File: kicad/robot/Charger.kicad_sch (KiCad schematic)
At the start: 32 parts, among them U13 MAX77976EFD+

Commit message: Added stock counts to parts I have
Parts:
- U13: Stock (none) -> 25
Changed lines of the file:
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@@
+      (effects (font (size 1.27 1.27)) hide)
+    )
+    (property "Stock" "25" (id 6) (at 121.92 106.68 0)
       (effects (font (size 1.27 1.27)) hide)
     )

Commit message: Batch BOM edits adding manufactuer and part numbers only
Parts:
- D5: Manufacturer (none) -> Nexperia
- D6: Manufacturer (none) -> Harvatek
- D7: Manufacturer (none) -> Vishay; manufacturer Vishay -> (none)
- L2: Manufacturer (none) -> Vishay
- R49: Manufacturer (none) -> Stackpole Electronics; Part Number (none) -> RMCF0603JG100K
- R50: Manufacturer (none) -> Stackpole Electronics; Part Number (none) -> RMCF0603JJ1K00
- R56: Manufacturer (none) -> Yageo; Part Number (none) -> RC0603JR-07110RL
- TP12: Manufacturer (none) -> N/A
- U13: Manufacturer (none) -> Maxim
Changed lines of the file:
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@@
+      (effects (font (size 1.27 1.27)) hide)
+    )
+    (property "Manufacturer" "Yageo" (id 5) (at 82.55 137.16 0)
+      (effects (font (size 1.27 1.27)) hide)
+    )
+    (property "Part Number" "RC0603JR-07110RL" (id 6) (at 82.55 137.16 0)
       (effects (font (size 1.27 1.27)) hide)
     )
@@
       (effects (font (size 1.27 1.27)) hide)
     )
+    (property "Manufacturer" "N/A" (id 6) (at 50.8 163.83 0)
+      (effects (font (size 1.27 1.27)) hide)
+    )
     (pin "1")
     (pin "2")
@@
     )
     (property "Description" "TVS Diode 20V" (id 5) (at 44.45 87.63 0)
+      (effects (font (size 1.27 1.27)) hide)
+    )
+    (property "Manufacturer" "Nexperia" (id 6) (at 44.45 87.63 0)
       (effects (font (size 1.27 1.27)) hide)
     )
@@
     )
     (property "Stock" "25" (id 6) (at 121.92 106.68 0)
+      (effects (font (size 1.27 1.27)) hide)
+    )
+    (property "Manufacturer" "Maxim" (id 7) (at 121.92 106.68 0)
       (effects (font (size 1.27 1.27)) hide)
     )
@@
       (effects (font (size 1.27 1.27)) hide)
     )
+    (property "Manufacturer" "Harvatek" (id 6) (at 72.39 137.16 0)
+      (effects (font (size 1.27 1.27)) hide)
+    )
     (pin "1")
     (pin "2")
@@
       (effects (font (size 1.27 1.27)) hide)
     )
+    (property "Manufacturer" "Vishay" (id 6) (at 171.45 99.06 0)
+      (effects (font (size 1.27 1.27)) hide)
+    )
     (pin "1")
     (pin "2")
@@
     )
     (property "Datasheet" "~" (id 3) (at 69.85 114.3 0)
+      (effects (font (size 1.27 1.27)) hide)
+    )
+    (property "Manufacturer" "Stackpole Electronics" (id 4) (at 69.85 114.3 0)
+      (effects (font (size 1.27 1.27)) hide)
+    )
+    (property "Part Number" "RMCF0603JG100K" (id 5) (at 69.85 114.3 0)
       (effects (font (size 1.27 1.27)) hide)
     )
@@
       (effects (font (size 1.27 1.27)) hide)
     )
+    (property "Manufacturer" "Stackpole Electronics" (id 4) (at 72.39 144.78 0)
+      (effects (font (size 1.27 1.27)) hide)
+    )
+    (property "Part Number" "RMCF0603JJ1K00" (id 5) (at 72.39 144.78 0)
+      (effects (font (size 1.27 1.27)) hide)
+    )
     (pin "1")
     (pin "2")
@@
       (effects (font (size 1.27 1.27)) (justify left) hide)
     )
-    (property "manufacturer" "Vishay" (id 15) (at 115.57 22.86 0)
+    (property "manufacturer" "" (id 15) (at 115.57 22.86 0)
       (effects (font (size 1.27 1.27)) (justify left) hide)
     )
@@
       (effects (font (size 1.27 1.27)) (justify left) hide)
     )
-    (pin "1")
+    (property "Manufacturer" "Vishay" (id 27) (at 115.57 63.5 0)
+      (effects (font (size 1.27 1.27)) hide)
+    )
+    (pin "1")

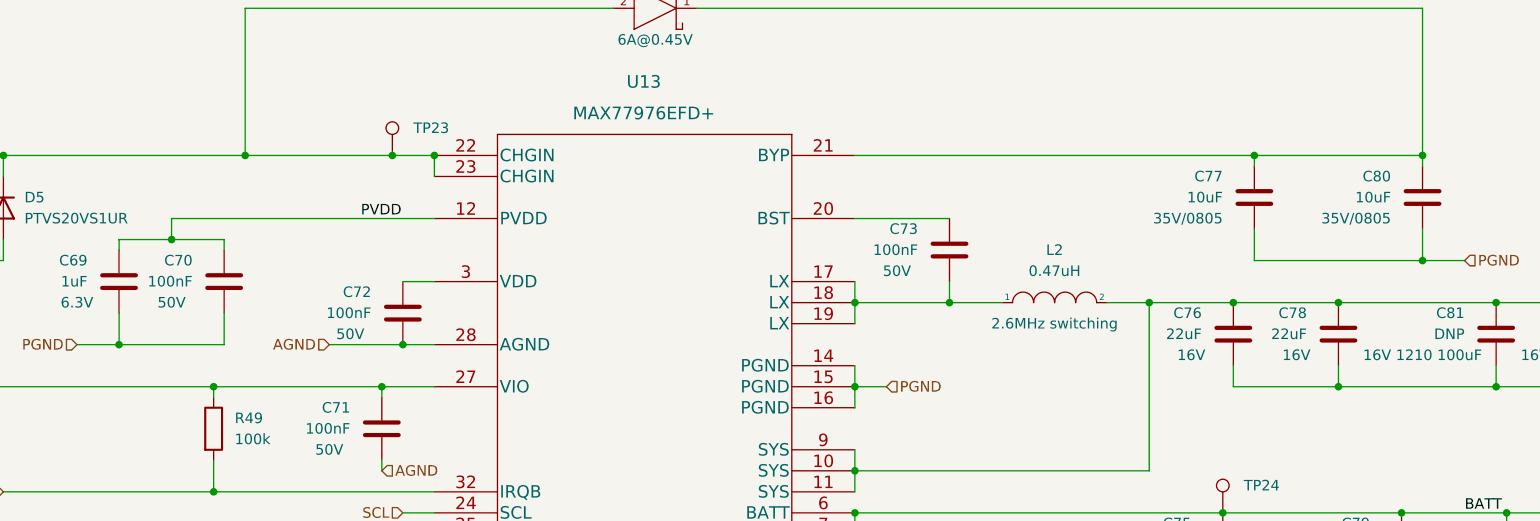
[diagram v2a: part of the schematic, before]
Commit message: bulk BOM edits. Mainly dealing with cap voltage ratings and part selection
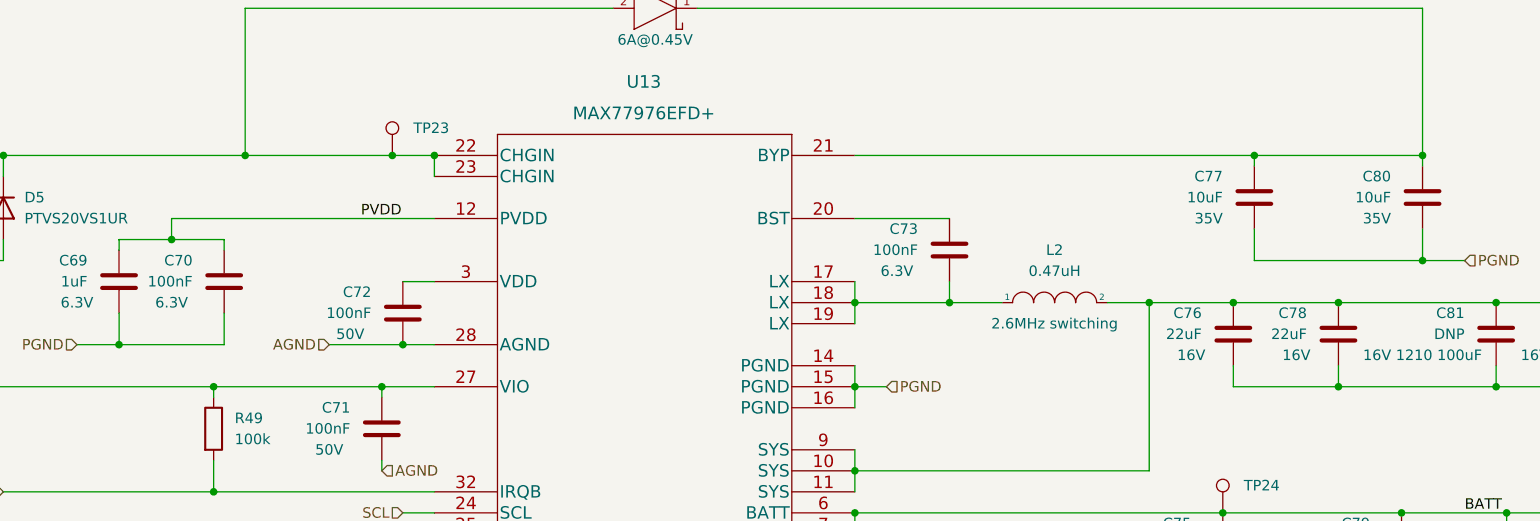
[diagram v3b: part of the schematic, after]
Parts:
- C67, C68, C77, C80: Manufacturer (none) -> Murata; Part Number (none) -> GRM21BR6YA106ME43L
- C69: Manufacturer (none) -> Samsung; Part Number (none) -> CL10A105KQ8NNNC
- C71, C72: Manufacturer (none) -> Samsung; Part Number (none) -> CL10B104MB8NNNC
- C75: Manufacturer (none) -> Samsung; Part Number (none) -> CL10A106MQ8NNNC
- C76, C78: Manufacturer (none) -> Samsung; Part Number (none) -> CL21A226MAQNNNF
- C79, C81, C82, C83: Manufacturer (none) -> N/A; Part Number (none) -> N/A
- D7: Part Number (none) -> SS1P3L
- JP7, JP8, JP9: Manufacturer (none) -> Adam Tech; Part Number (none) -> PH1-02-UA
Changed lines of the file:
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@@
       (effects (font (size 1.27 1.27)) (justify left))
+    )
+    (property "Manufacturer" "Samsung" (id 5) (at 191.77 128.27 0)
+      (effects (font (size 1.27 1.27)) hide)
+    )
+    (property "Part Number" "CL10A106MQ8NNNC" (id 6) (at 191.77 128.27 0)
+      (effects (font (size 1.27 1.27)) hide)
     )
     (pin "1")
@@
     )
     (property "Description" "50V" (id 4) (at 86.36 102.87 0))
+    (property "Manufacturer" "Samsung" (id 5) (at 92.71 100.33 0)
+      (effects (font (size 1.27 1.27)) hide)
+    )
+    (property "Part Number" "CL10B104MB8NNNC" (id 6) (at 92.71 100.33 0)
+      (effects (font (size 1.27 1.27)) hide)
+    )
     (pin "1")
     (pin "2")
@@
     )
     (property "Description" "16V 1210 100uF" (id 4) (at 255.27 105.41 0))
+    (property "Manufacturer" "N/A" (id 5) (at 264.16 102.87 0)
+      (effects (font (size 1.27 1.27)) hide)
+    )
+    (property "Part Number" "N/A" (id 6) (at 264.16 102.87 0)
+      (effects (font (size 1.27 1.27)) hide)
+    )
     (pin "1")
     (pin "2")
@@
     )
     (property "Description" "50V" (id 4) (at 83.82 116.84 0))
+    (property "Manufacturer" "Samsung" (id 5) (at 90.17 114.3 0)
+      (effects (font (size 1.27 1.27)) hide)
+    )
+    (property "Part Number" "CL10B104MB8NNNC" (id 6) (at 90.17 114.3 0)
+      (effects (font (size 1.27 1.27)) hide)
+    )
     (pin "1")
     (pin "2")
@@
     (property "Description" "35V" (id 4) (at 34.29 88.8999 0)
       (effects (font (size 1.27 1.27)) (justify left))
+    )
+    (property "Manufacturer" "Murata" (id 5) (at 30.48 86.36 0)
+      (effects (font (size 1.27 1.27)) hide)
+    )
+    (property "Part Number" "GRM21BR6YA106ME43L" (id 6) (at 30.48 86.36 0)
+      (effects (font (size 1.27 1.27)) hide)
     )
     (pin "1")
@@
     )
     (property "Description" "16V 1210 100uF" (id 4) (at 215.9 105.41 0))
+    (property "Manufacturer" "N/A" (id 5) (at 224.79 102.87 0)
+      (effects (font (size 1.27 1.27)) hide)
+    )
+    (property "Part Number" "N/A" (id 6) (at 224.79 102.87 0)
+      (effects (font (size 1.27 1.27)) hide)
+    )
     (pin "1")
     (pin "2")
@@
       (effects (font (size 1.27 1.27)) hide)
     )
-    (property "Description" "50V" (id 4) (at 64.77 99.06 0))
+    (property "Description" "6.3V" (id 4) (at 64.77 99.06 0))
     (pin "1")
     (pin "2")
@@
     )
     (property "Description" "16V" (id 4) (at 187.96 105.41 0))
+    (property "Manufacturer" "Samsung" (id 5) (at 193.04 102.87 0)
+      (effects (font (size 1.27 1.27)) hide)
+    )
+    (property "Part Number" "CL21A226MAQNNNF" (id 6) (at 193.04 102.87 0)
+      (effects (font (size 1.27 1.27)) hide)
+    )
     (pin "1")
     (pin "2")
@@
       (effects (font (size 1.27 1.27)) hide)
     )
+    (property "Manufacturer" "Adam Tech" (id 5) (at 43.18 137.16 0)
+      (effects (font (size 1.27 1.27)) hide)
+    )
+    (property "Part Number" "PH1-02-UA" (id 6) (at 43.18 137.16 0)
+      (effects (font (size 1.27 1.27)) hide)
+    )
     (pin "1")
     (pin "2")
@@
       (effects (font (size 1.27 1.27)) hide)
     )
+    (property "Manufacturer" "Adam Tech" (id 5) (at 43.18 148.59 0)
+      (effects (font (size 1.27 1.27)) hide)
+    )
+    (property "Part Number" "PH1-02-UA" (id 6) (at 43.18 148.59 0)
+      (effects (font (size 1.27 1.27)) hide)
+    )
     (pin "1")
     (pin "2")
@@
     )
     (property "Description" "16V" (id 4) (at 200.66 105.41 0))
+    (property "Manufacturer" "Samsung" (id 5) (at 205.74 102.87 0)
+      (effects (font (size 1.27 1.27)) hide)
+    )
+    (property "Part Number" "CL21A226MAQNNNF" (id 6) (at 205.74 102.87 0)
+      (effects (font (size 1.27 1.27)) hide)
+    )
     (pin "1")
     (pin "2")
@@
       (effects (font (size 1.27 1.27)) hide)
     )
+    (property "Manufacturer" "Adam Tech" (id 5) (at 33.02 109.22 0)
+      (effects (font (size 1.27 1.27)) hide)
+    )
+    (property "Part Number" "PH1-02-UA" (id 6) (at 33.02 109.22 0)
+      (effects (font (size 1.27 1.27)) hide)
+    )
     (pin "1")
     (pin "2")
@@
       (effects (font (size 1.27 1.27)) (justify left))
     )
+    (property "Manufacturer" "Murata" (id 5) (at 17.78 86.36 0)
+      (effects (font (size 1.27 1.27)) hide)
+    )
+    (property "Part Number" "GRM21BR6YA106ME43L" (id 6) (at 17.78 86.36 0)
+      (effects (font (size 1.27 1.27)) hide)
+    )
     (pin "1")
     (pin "2")
@@
       (effects (font (size 1.27 1.27)) hide)
     )
-    (property "Description" "35V/0805" (id 4) (at 212.09 88.8999 0)
-      (effects (font (size 1.27 1.27)) (justify left))
+    (property "Description" "35V" (id 4) (at 212.09 88.8999 0)
+      (effects (font (size 1.27 1.27)) (justify left))
+    )
+    (property "Manufacturer" "Murata" (id 5) (at 215.9 86.36 0)
+      (effects (font (size 1.27 1.27)) hide)
+    )
+    (property "Part Number" "GRM21BR6YA106ME43L" (id 6) (at 215.9 86.36 0)
+      (effects (font (size 1.27 1.27)) hide)
     )
     (pin "1")
@@
     )
     (property "Description" "6.3V" (id 4) (at 53.34 99.06 0))
+    (property "Manufacturer" "Samsung" (id 5) (at 58.42 96.52 0)
+      (effects (font (size 1.27 1.27)) hide)
+    )
+    (property "Part Number" "CL10A105KQ8NNNC" (id 6) (at 58.42 96.52 0)
+      (effects (font (size 1.27 1.27)) hide)
+    )
     (pin "1")
     (pin "2")
@@
     )
     (property "Description" "16V 1210 100uF" (id 4) (at 234.95 105.41 0))
+    (property "Manufacturer" "N/A" (id 5) (at 243.84 102.87 0)
+      (effects (font (size 1.27 1.27)) hide)
+    )
+    (property "Part Number" "N/A" (id 6) (at 243.84 102.87 0)
+      (effects (font (size 1.27 1.27)) hide)
+    )
     (pin "1")
     (pin "2")
@@
       (effects (font (size 1.27 1.27)) hide)
     )
-    (property "Description" "35V/0805" (id 4) (at 191.77 88.8999 0)
-      (effects (font (size 1.27 1.27)) (justify left))
+    (property "Description" "35V" (id 4) (at 191.77 88.8999 0)
+      (effects (font (size 1.27 1.27)) (justify left))
+    )
+    (property "Manufacturer" "Murata" (id 5) (at 195.58 86.36 0)
+      (effects (font (size 1.27 1.27)) hide)
+    )
+    (property "Part Number" "GRM21BR6YA106ME43L" (id 6) (at 195.58 86.36 0)
+      (effects (font (size 1.27 1.27)) hide)
     )
     (pin "1")
@@
       (effects (font (size 1.27 1.27)) hide)
     )
+    (property "Part Number" "SS1P3L" (id 28) (at 115.57 63.5 0)
+      (effects (font (size 1.27 1.27)) hide)
+    )
     (pin "1")
     (pin "2")
@@
     )
     (property "Description" "16V 1210 220uF" (id 4) (at 204.47 130.81 0))
+    (property "Manufacturer" "N/A" (id 5) (at 213.36 128.27 0)
+      (effects (font (size 1.27 1.27)) hide)
+    )
+    (property "Part Number" "N/A" (id 6) (at 213.36 128.27 0)
+      (effects (font (size 1.27 1.27)) hide)
+    )
     (pin "1")
     (pin "2")
@@
       (effects (font (size 1.27 1.27)) hide)
     )
-    (property "Description" "50V" (id 4) (at 152.4 95.25 0))
-    (pin "1")
-    (pin "2")
+    (property "Description" "6.3V" (id 4) (at 152.4 95.25 0))
+    (pin "1")
+    (pin "2")

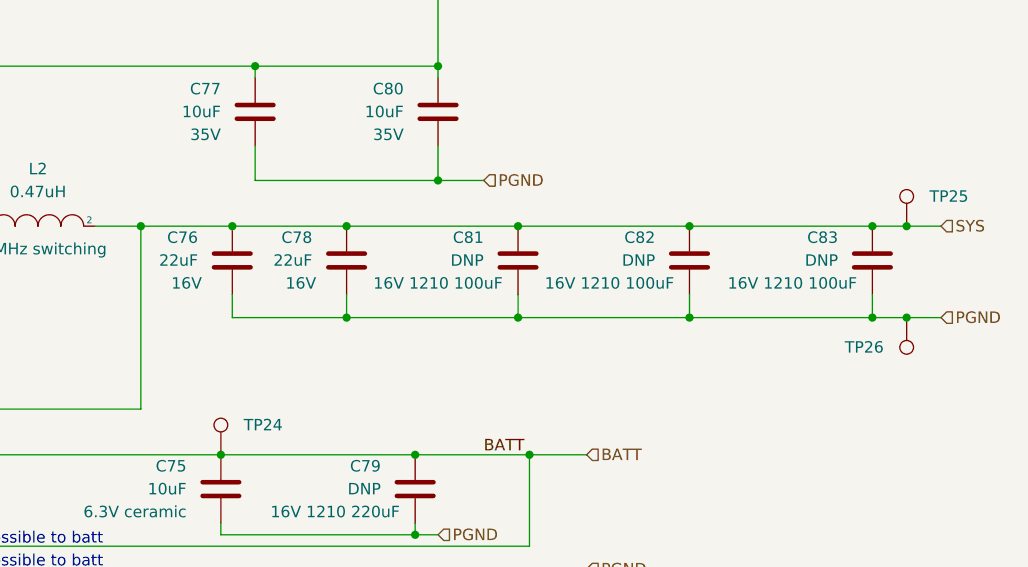
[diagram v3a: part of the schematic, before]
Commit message: Replaced DNP 1210 caps with onboard 0603 DNP caps on backside
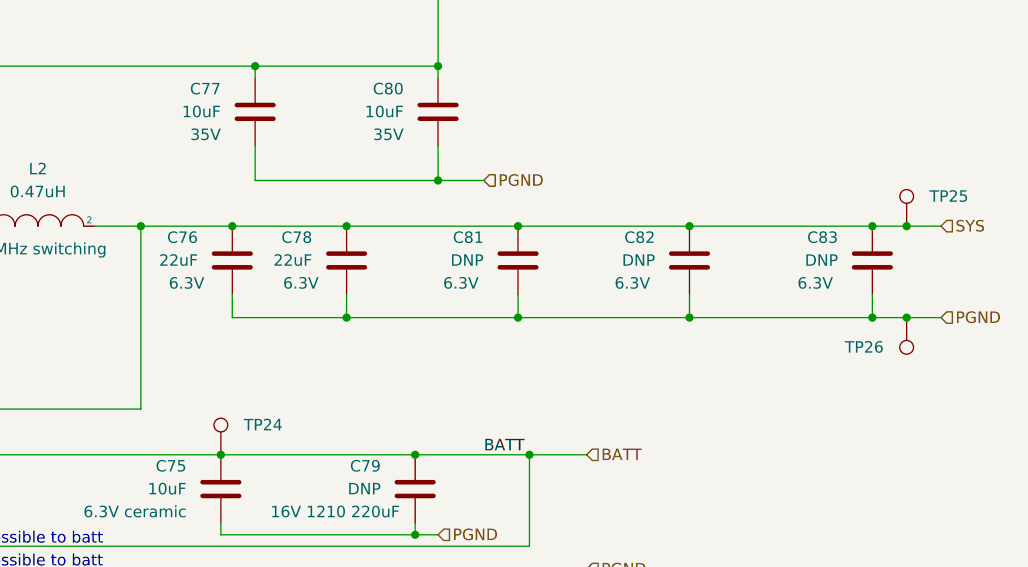
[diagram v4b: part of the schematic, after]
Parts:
- C76, C78: Manufacturer Samsung -> (none); Part Number CL21A226MAQNNNF -> (none)
- C81, C82, C83: footprint Capacitor_SMD:C_1210_3225Metric -> Capacitor_SMD:C_0805_2012Metric; now left out of the parts list
